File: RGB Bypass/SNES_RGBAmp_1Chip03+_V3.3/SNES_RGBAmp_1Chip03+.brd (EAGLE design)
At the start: 31.1 x 20.5 mm, 30 parts

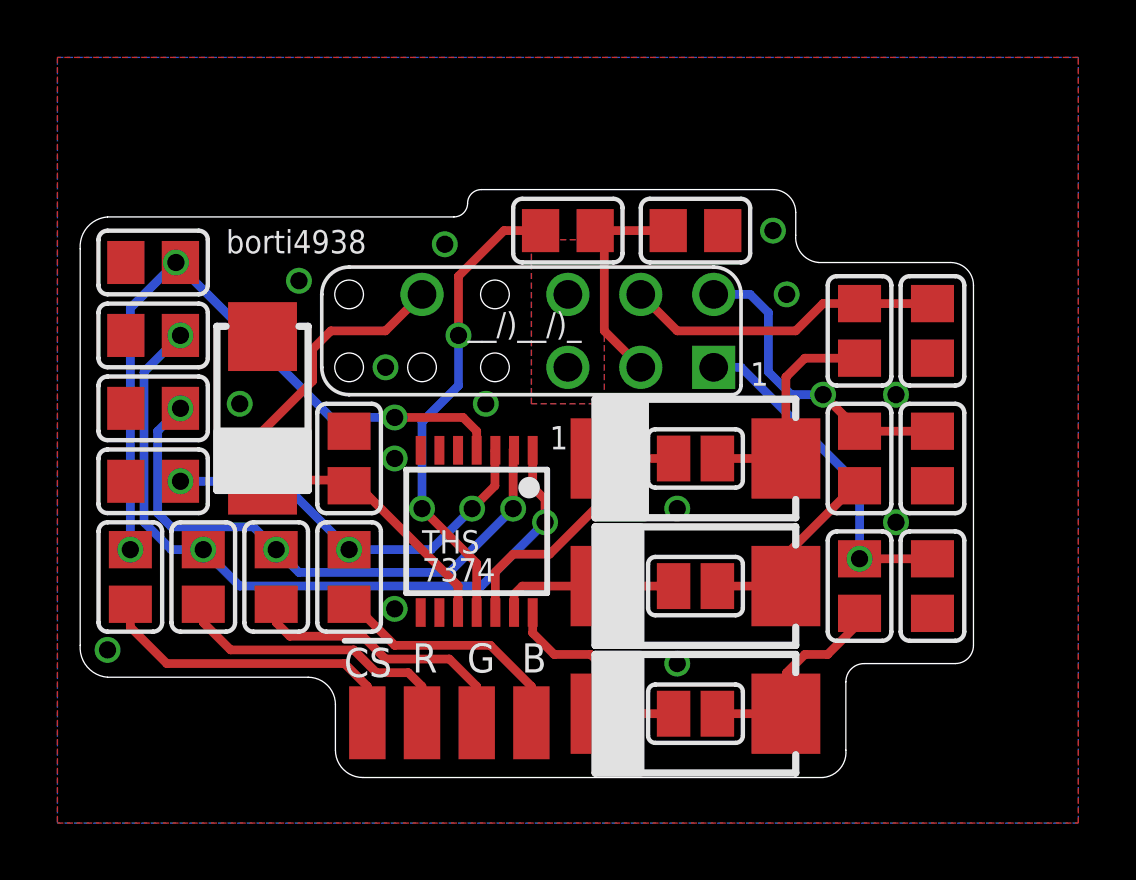
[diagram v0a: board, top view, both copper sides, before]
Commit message: Update: 330uF tantalum in CSYNC line at the output of the THS7374.
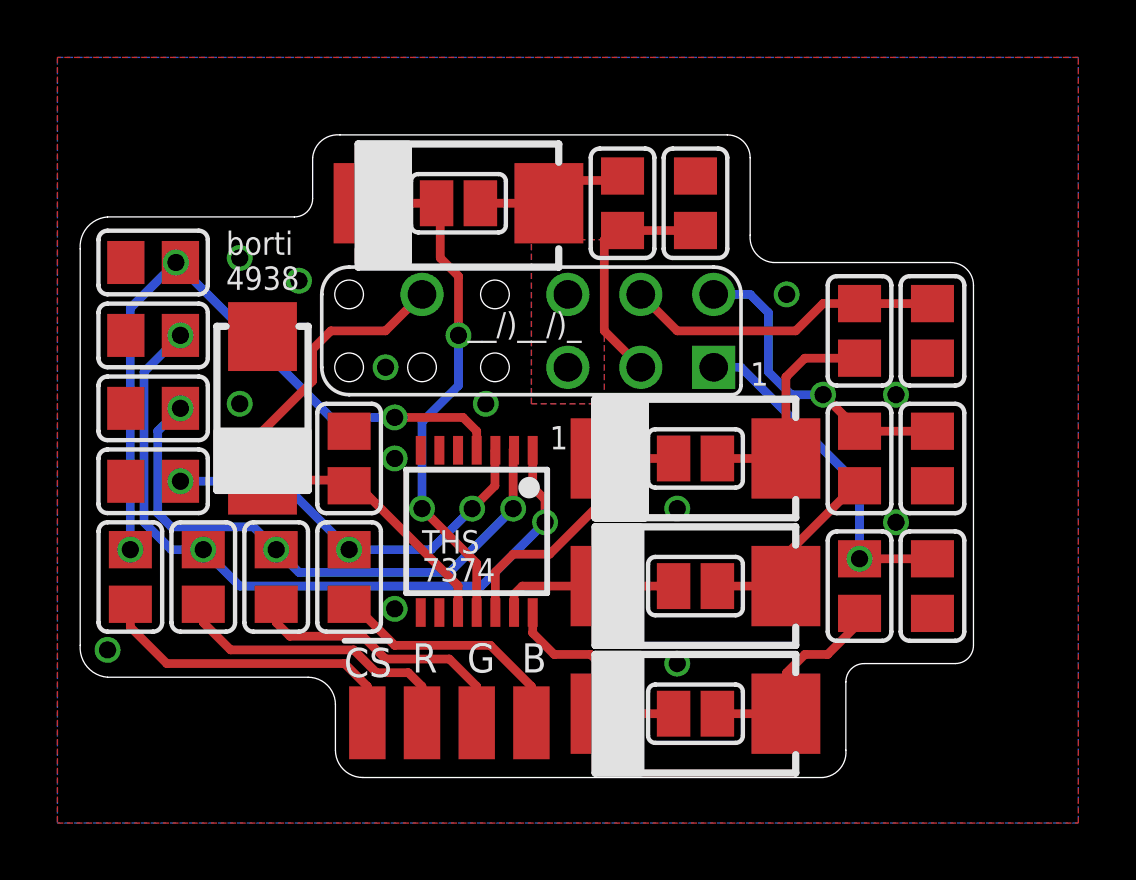
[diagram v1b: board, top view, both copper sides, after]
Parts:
- added C10: 330u, rcl:SMC_D
- added SJ4: (no value), jumper:SJ
- moved R15 2.13 mm to (29.8, 43.2), turned to 270 degrees
- moved C7 0.95 mm to (32.4, 43.2), turned to 90 degrees
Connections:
- new net N$19: C10.-, R15.1, SJ4.2
- net N$18: now also C10.+, SJ4.1; no longer R15.1
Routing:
- net N$19: track 0.00 -> 5.80 mm
- net N$18: track 16.5 -> 18.3 mm
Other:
- board size 31.1 x 20.5 mm -> 31.1 x 22.4 mm
- board text added: "C6 (330uF/ 6.3V )"
- board text added: "borti 4938"
- board text removed: "borti4938"
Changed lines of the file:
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@@
 <?xml version="1.0" encoding="utf-8"?>
 <!DOCTYPE eagle SYSTEM "eagle.dtd">
-<eagle version="7.4.0">
+<eagle version="7.5.0">
 <drawing>
 <settings>
@@
 <wire x1="28.8925" y1="32.86125" x2="28.8925" y2="32.22625" width="0.254" layer="21"/>
 <wire x1="28.8925" y1="35.71875" x2="28.8925" y2="36.35375" width="0.254" layer="21"/>
-<wire x1="28.8925" y1="36.35375" x2="35.8775" y2="36.35375" width="0.254" layer="21"/>
 <wire x1="35.8775" y1="36.35375" x2="35.8775" y2="35.71875" width="0.254" layer="21"/>
 <wire x1="28.8925" y1="31.27375" x2="28.8925" y2="31.90875" width="0.254" layer="21"/>
@@
 <text x="22.86" y="30.00375" size="0.8128" layer="21" font="vector" ratio="15" distance="20">THS
 7374</text>
-<wire x1="11.90625" y1="42.70375" x2="23.97125" y2="42.70375" width="0" layer="20"/>
-<wire x1="24.92375" y1="43.65625" x2="35.08375" y2="43.65625" width="0" layer="20"/>
-<wire x1="35.08375" y1="43.65625" x2="35.8775" y2="42.8625" width="0" layer="20" curve="-90"/>
-<wire x1="35.8775" y1="42.8625" x2="35.8775" y2="42.06875" width="0" layer="20"/>
-<wire x1="35.8775" y1="42.06875" x2="36.67125" y2="41.11625" width="0" layer="20" curve="90"/>
-<wire x1="36.67125" y1="41.11625" x2="41.275" y2="41.11625" width="0" layer="20"/>
+<wire x1="11.90625" y1="42.70375" x2="18.415" y2="42.70375" width="0" layer="20"/>
+<wire x1="20.0025" y1="45.56125" x2="33.49625" y2="45.56125" width="0" layer="20"/>
+<wire x1="33.49625" y1="45.56125" x2="34.29" y2="44.7675" width="0" layer="20" curve="-90"/>
+<wire x1="34.29" y1="44.7675" x2="34.29" y2="42.06875" width="0" layer="20"/>
+<wire x1="34.29" y1="42.06875" x2="35.08375" y2="41.11625" width="0" layer="20" curve="90"/>
+<wire x1="35.08375" y1="41.11625" x2="41.275" y2="41.11625" width="0" layer="20"/>
 <text x="18.415" y="29.21" size="0.8128" layer="26" font="vector" ratio="15" distance="20" rot="MR0">R5</text>
 <text x="20.955" y="29.21" size="0.8128" layer="26" font="vector" ratio="15" distance="20" rot="MR0">R6</text>
@@
 <text x="21.11375" y="27.94" size="0.8128" layer="26" font="vector" ratio="15" distance="20" rot="MR0">(1.3kΩ)</text>
 <text x="16.03375" y="37.1475" size="0.8128" layer="26" font="vector" ratio="15" distance="20" rot="MR0">(9.53kΩ)</text>
-<text x="30.63875" y="43.18" size="0.8128" layer="26" font="vector" ratio="15" distance="20" rot="MR180"> C10
+<text x="31.59125" y="41.275" size="0.8128" layer="26" font="vector" ratio="15" distance="20" rot="MR90"> C10
 (47pF)</text>
-<text x="28.09875" y="42.70375" size="0.8128" layer="26" font="vector" ratio="15" distance="20" rot="MR180">R10</text>
+<text x="30.00375" y="42.06875" size="0.8128" layer="26" font="vector" ratio="15" distance="20" rot="MR90">R10</text>
 <text x="12.85875" y="28.73375" size="0.8128" layer="26" font="vector" ratio="15" distance="20" rot="MR90">R11</text>
 <text x="13.6525" y="41.11625" size="0.8128" layer="26" font="vector" ratio="15" distance="20" rot="MR0">R12</text>
@@
 <text x="11.58875" y="28.09875" size="0.8128" layer="26" font="vector" ratio="15" distance="20" rot="MR90">(5.0kΩ)</text>
 <wire x1="20.16125" y1="27.94" x2="21.74875" y2="27.94" width="0.2032" layer="25"/>
-<wire x1="23.97125" y1="42.70375" x2="24.4475" y2="43.18" width="0" layer="20" curve="90"/>
-<wire x1="24.4475" y1="43.18" x2="24.92375" y2="43.65625" width="0" layer="20" curve="-90"/>
-<text x="16.03375" y="41.43375" size="0.8128" layer="21" font="vector" ratio="15">borti4938</text>
+<wire x1="18.415" y1="42.70375" x2="19.05" y2="43.33875" width="0" layer="20" curve="90"/>
+<text x="16.03375" y="40.16375" size="0.8128" layer="21" font="vector" ratio="15">borti
+4938</text>
 <text x="13.97" y="28.2575" size="0.8128" layer="26" font="vector" ratio="15" distance="20" rot="MR90">(806Ω)</text>
 <text x="11.58875" y="32.22625" size="0.8128" layer="26" font="vector" ratio="15" distance="20" rot="MR90">(8.45kΩ)</text>
@@
 <text x="39.6875" y="29.5275" size="0.8128" layer="26" font="vector" ratio="15" distance="20" rot="MR90">C7-C9 (47pF)
 (Jr./Mini only)</text>
-<text x="24.60625" y="43.18" size="0.8128" layer="26" font="vector" ratio="15" distance="20" rot="MR180">(75Ω-
+<text x="27.94" y="41.43375" size="0.8128" layer="26" font="vector" ratio="15" distance="20" rot="MR90">(75Ω-
 300Ω)</text>
+<wire x1="19.05" y1="43.33875" x2="19.05" y2="44.7675" width="0" layer="20"/>
+<wire x1="19.05" y1="44.7675" x2="20.0025" y2="45.56125" width="0" layer="20" curve="-90"/>
+<text x="26.51125" y="41.91" size="0.8128" layer="26" font="vector" ratio="15" distance="20" rot="MR0">  C6
+(330uF/
+ 6.3V  )</text>
+<wire x1="28.8925" y1="36.35375" x2="35.8775" y2="36.35375" width="0.254" layer="21"/>
+<wire x1="20.6375" y1="40.9575" x2="27.6225" y2="40.9575" width="0.254" layer="21"/>
+<wire x1="27.6225" y1="41.5925" x2="27.6225" y2="40.9575" width="0.254" layer="21"/>
+<wire x1="27.6225" y1="45.24375" x2="27.6225" y2="44.60875" width="0.254" layer="21"/>
+<wire x1="20.6375" y1="45.24375" x2="27.6225" y2="45.24375" width="0.254" layer="21"/>
+<wire x1="20.6375" y1="45.24375" x2="20.6375" y2="44.60875" width="0.254" layer="21"/>
+<wire x1="20.6375" y1="41.5925" x2="20.6375" y2="40.9575" width="0.254" layer="21"/>
+<polygon width="0.254" layer="21">
+<vertex x="28.8925" y="36.35375"/>
+<vertex x="30.63875" y="36.35375"/>
+<vertex x="30.63875" y="32.22625"/>
+<vertex x="28.8925" y="32.22625"/>
+</polygon>
+<polygon width="0.254" layer="21">
+<vertex x="28.8925" y="36.35375"/>
+<vertex x="30.63875" y="36.35375"/>
+<vertex x="30.63875" y="32.22625"/>
+<vertex x="28.8925" y="32.22625"/>
+</polygon>
+<polygon width="0.254" layer="21">
+<vertex x="20.6375" y="45.24375"/>
+<vertex x="22.38375" y="45.24375"/>
+<vertex x="22.38375" y="41.11625"/>
+<vertex x="20.6375" y="41.11625"/>
+</polygon>
 </plain>
 <attributes>
@@
 </element>
 <element name="R14" library="snescart" package="Z0805" value="75" x="13.49375" y="41.11625" smashed="yes"/>
-<element name="R15" library="snescart" package="Z0805" value="75" x="27.94" y="42.2275" smashed="yes"/>
-<element name="C7" library="snescart" package="Z0805" value="100n" x="32.385" y="42.2275" smashed="yes"/>
+<element name="R15" library="snescart" package="Z0805" value="75" x="29.845" y="43.18" smashed="yes" rot="R270"/>
+<element name="C7" library="snescart" package="Z0805" value="100n" x="32.385" y="43.18" smashed="yes" rot="R90"/>
 <element name="C6" library="snescart" package="Z0805" value="100n" x="40.64" y="29.845" smashed="yes" rot="R270"/>
 <element name="C8" library="snescart" package="Z0805" value="100n" x="40.64" y="34.29" smashed="yes" rot="R270"/>
 <element name="C9" library="snescart" package="Z0805" value="100n" x="40.64" y="38.735" smashed="yes" rot="R270"/>
+<element name="C10" library="rcl" package="SMC_D" value="330u" x="24.13" y="43.18" smashed="yes"/>
+<element name="SJ4" library="jumper" package="SJ" value="" x="24.13" y="43.18" smashed="yes">
+<attribute name="VALUE" x="24.5301" y="43.18" size="0.02" layer="27"/>
+</element>
 </elements>
 <signals>
@@
 <via x="16.51" y="36.195" extent="1-16" drill="0.6"/>
 <via x="11.90625" y="27.6225" extent="1-16" drill="0.6"/>
-<via x="35.08375" y="42.2275" extent="1-16" drill="0.6"/>
+<via x="16.51" y="41.275" extent="1-16" drill="0.6"/>
 <contactref element="C6" pad="2"/>
 <contactref element="C8" pad="2"/>
@@
 <via x="39.37" y="32.0675" extent="1-16" drill="0.6"/>
 <via x="39.37" y="36.5125" extent="1-16" drill="0.6"/>
-<via x="23.65375" y="41.75125" extent="1-16" drill="0.6"/>
 </signal>
 <signal name="VCC">
@@
 <contactref element="U$3" pad="P$3"/>
 <contactref element="C7" pad="1"/>
-<wire x1="28.89" y1="42.2275" x2="31.435" y2="42.2275" width="0.3048" layer="1"/>
+<wire x1="29.845" y1="42.23" x2="32.385" y2="42.23" width="0.3048" layer="1"/>
 <wire x1="30.48" y1="37.465" x2="29.21" y2="38.735" width="0.3048" layer="1"/>
 <wire x1="29.21" y1="38.735" x2="29.21" y2="41.9075" width="0.3048" layer="1"/>
-<wire x1="29.21" y1="41.9075" x2="28.89" y2="42.2275" width="0.3048" layer="1"/>
+<wire x1="29.21" y1="41.9075" x2="29.845" y2="42.23" width="0.3048" layer="1"/>
 </signal>
 <signal name="N$18">
-<contactref element="R15" pad="1"/>
 <contactref element="U$2" pad="11"/>
 <wire x1="24.765" y1="28.925" x2="24.765" y2="30.63875" width="0.3048" layer="1"/>
@@
 <via x="24.13" y="38.57625" extent="1-16" drill="0.6"/>
 <wire x1="24.13" y1="38.57625" x2="24.13" y2="40.64" width="0.3048" layer="1"/>
-<wire x1="26.99" y1="42.2275" x2="25.7175" y2="42.2275" width="0.3048" layer="1"/>
-<wire x1="25.7175" y1="42.2275" x2="24.13" y2="40.64" width="0.3048" layer="1"/>
+<contactref element="C10" pad="+"/>
+<contactref element="SJ4" pad="1"/>
+<wire x1="24.13" y1="40.64" x2="23.495" y2="41.275" width="0.3048" layer="1"/>
+<wire x1="23.495" y1="41.275" x2="23.495" y2="43.053" width="0.3048" layer="1"/>
+<wire x1="23.495" y1="43.053" x2="23.368" y2="43.18" width="0.3048" layer="1"/>
+<wire x1="20.98" y1="43.18" x2="23.368" y2="43.18" width="0.3048" layer="1"/>
+</signal>
+<signal name="N$19">
+<contactref element="R15" pad="1"/>
+<contactref element="C10" pad="-"/>
+<contactref element="SJ4" pad="2"/>
+<wire x1="27.28" y1="43.18" x2="24.892" y2="43.18" width="0.3048" layer="1"/>
+<wire x1="29.845" y1="44.13" x2="29.845" y2="43.97375" width="0.3048" layer="1"/>
+<wire x1="29.845" y1="43.97375" x2="27.46375" y2="43.97375" width="0.3048" layer="1"/>
+<wire x1="27.46375" y1="43.97375" x2="27.305" y2="43.815" width="0.3048" layer="1"/>
+<wire x1="27.305" y1="43.815" x2="27.305" y2="43.205" width="0.3048" layer="1"/>
+<wire x1="27.305" y1="43.205" x2="27.28" y2="43.18" width="0.3048" layer="1"/>
 </signal>
 </signals>
